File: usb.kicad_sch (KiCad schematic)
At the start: 29 parts, among them J3 USB-C_USB4105-GF-A, U11 TPD4E05U06QDQARQ1, U5 FT230X_QFN, U8 NCP730BMT330_WSON

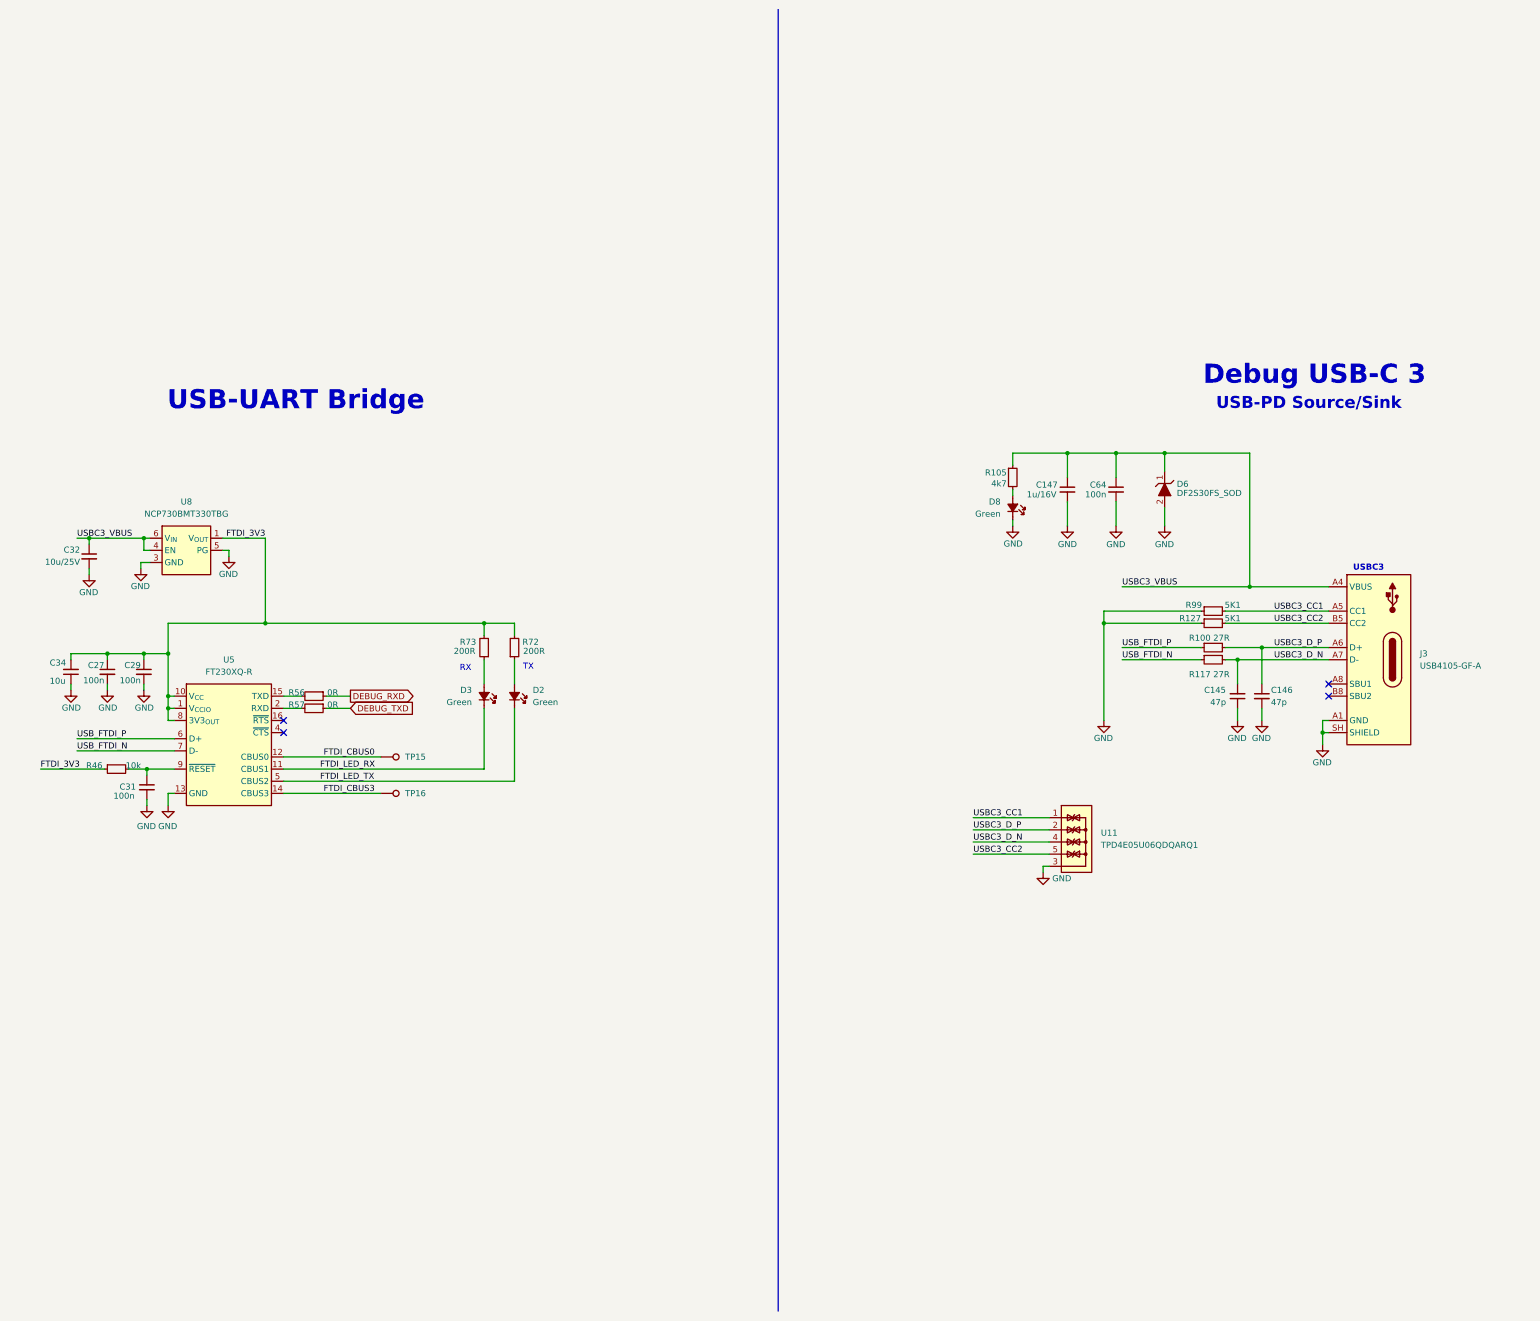
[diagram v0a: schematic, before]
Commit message: Schematic Cleanup, Complete routing
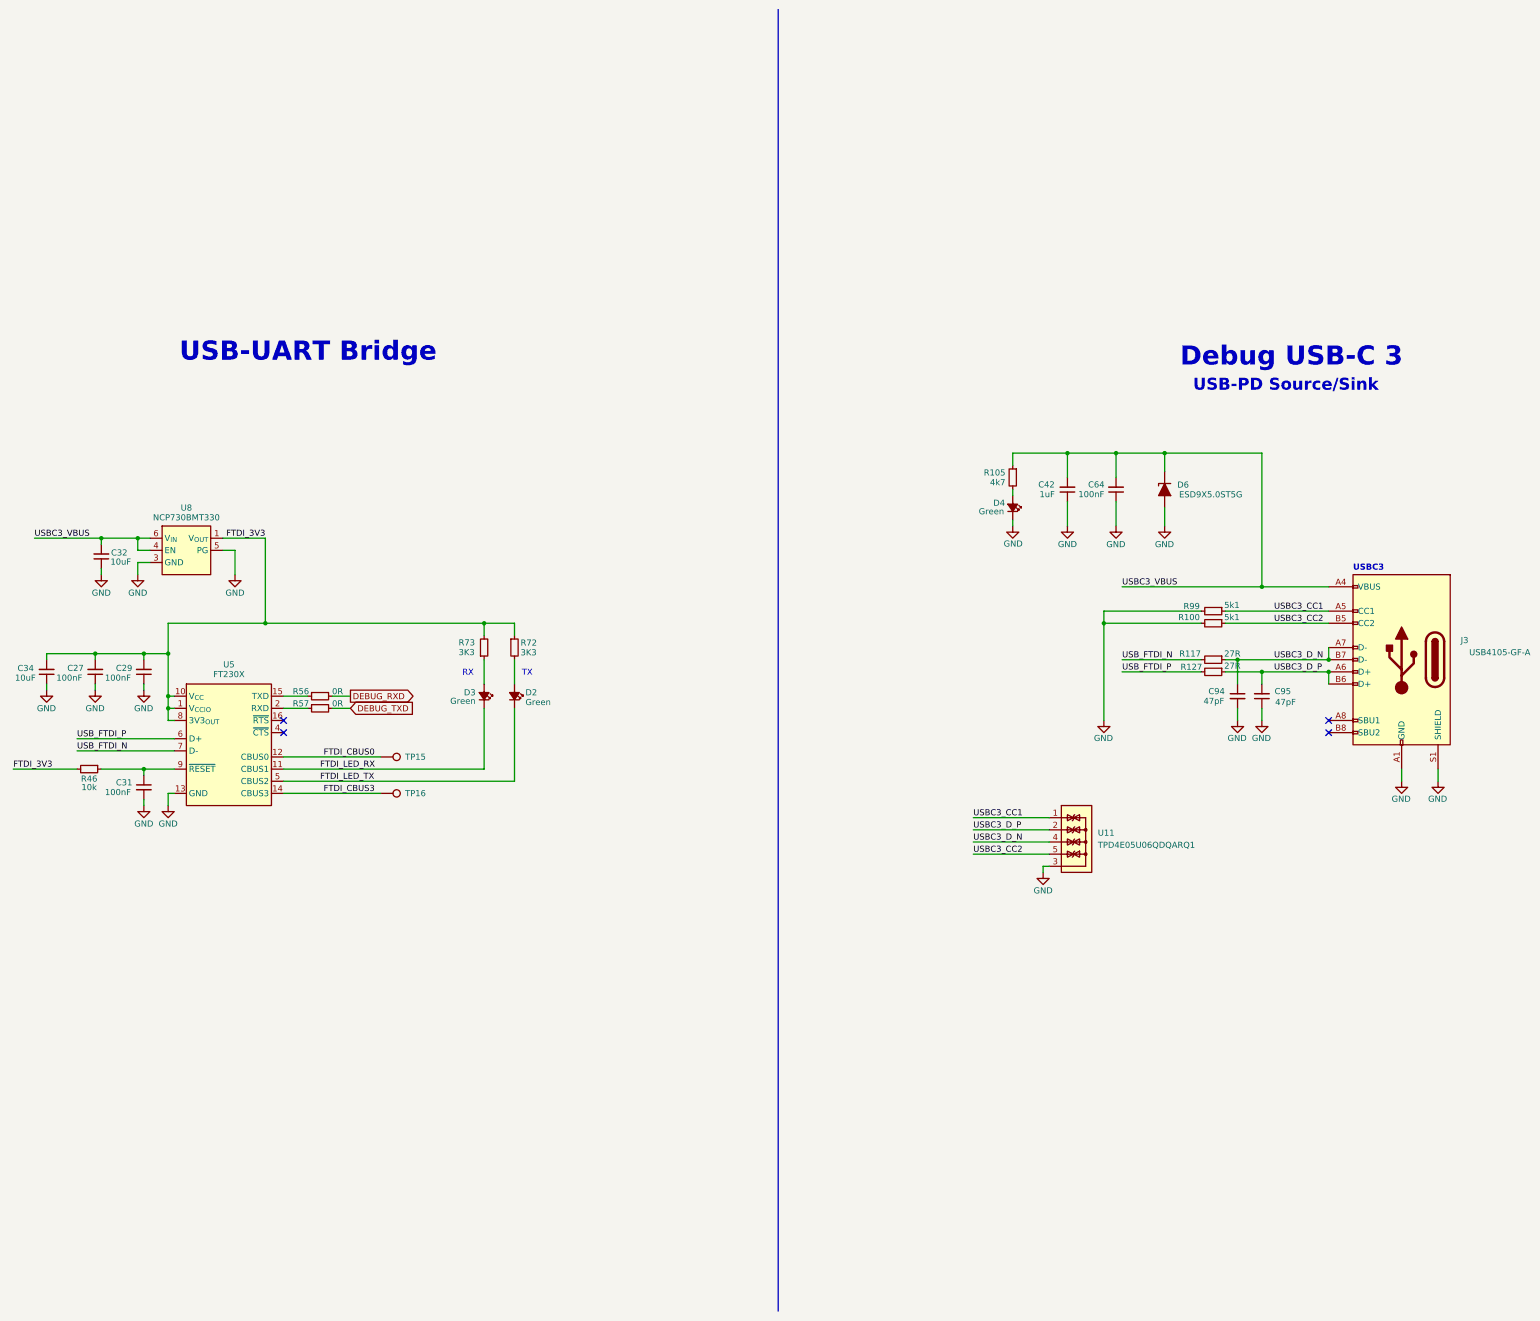
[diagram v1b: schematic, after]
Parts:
- C27, C29, C31, C64: value C_100n_0603 -> 100nF; symbol antmicroCapacitors0402:C_100n_0402 -> Device:C_Small
- C32: value C_10u_25V_0603 -> 10uF; symbol antmicroCapacitors0603:C_10u_25V_0603 -> Device:C_Small
- C34: value C_10u_0603 -> 10uF; symbol antmicroCapacitors0402:C_10u_0402 -> Device:C_Small
- C42: renamed from C147; value C_1u_16V_0603 -> 1uF; symbol antmicroCapacitors0402:C_1u_16V_0402 -> Device:C_Small
- C94: renamed from C145; value C_47p_0402 -> 47pF; symbol antmicroCapacitors0402:C_47p_0402 -> Device:C_Small
- C95: renamed from C146; value C_47p_0402 -> 47pF; symbol antmicroCapacitors0402:C_47p_0402 -> Device:C_Small
- D2, D3: symbol antmicroLEDIndicationDiscrete:LED_G_0603_LTST-C190GKT -> Device:LED_Small_Filled
- D4: renamed from D8; symbol antmicroLEDIndicationDiscrete:LED_G_0603_LTST-C190GKT -> Device:LED_Small_Filled
- D6: value DF2S30FS_SOD -> ESD9X5.0ST5G; symbol antmicroTVSDiodes:DF2S30FS_SOD -> Device:D_Zener_Filled
- J3: value USB-C_USB4105-GF-A -> USB4105-GF-A; symbol antmicroUSBConnectors:USB-C_GCT_USB4105-GF-A -> Connector:USB_C_Receptacle_USB2.0_16P
- R100: value R_5K1_0402 -> 5k1; symbol antmicroResistors0402:R_27R_0402 -> Device:R_Small; MPN CR0402-FX-27R0GLF -> (none); Manufacturer Bourns -> (none); Val 27R -> (none)
- R105: value R_4k7_0603 -> 4k7; symbol antmicroResistors0402:R_4k7_0402 -> Device:R_Small
- R117: value R_27R_0603 -> 27R; symbol antmicroResistors0402:R_27R_0402 -> Device:R_Small
- R127: value R_27R_0603 -> 27R; symbol antmicroResistors0402:R_27R_0402 -> Device:R_Small; Val 5K1 -> (none)
- R46: value R_10k_0603 -> 10k; symbol antmicroResistors0402:R_10k_0402 -> Device:R_Small
- R56, R57: value R_0R_0402 -> 0R; symbol antmicroResistors0402:R_0R_0402 -> Device:R_Small
- R72, R73: value R_200R_0603 -> 3K3; symbol antmicroResistors0402:R_200R_0402 -> Device:R_Small; MPN CR0402-FX-2000GLF -> (none); Manufacturer Bourns -> (none); Val 200R -> 3K3
- R99: value R_5K1_0603 -> 5k1; symbol antmicroResistors0402:R_27R_0402 -> Device:R_Small; MPN CR0402-FX-27R0GLF -> (none); Val 5K1 -> (none)
- TP15, TP16: symbol antmicroTestPoints:TP_0.75mm_SMD -> Connector:TestPoint
- U11: symbol antmicroTVSDiodes:TPD4E05U06QDQARQ1 -> JetsonCarrier:TPD4E05U06QDQARQ1
- U5: value FT230X_QFN -> FT230X; symbol antmicroInterfaceControllers:FT230X_QFN -> JetsonCarrier:FT230XQ
- U8: value NCP730BMT330_WSON -> NCP730BMT330; symbol antmicroPMICVoltageRegulatorsLinear:NCP730BMT330_WSON -> JetsonCarrier:NCP730BMT330
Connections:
- net DEBUG_RXD: now also R56.2; no longer R56.1
- net DEBUG_TXD: now also R57.2; no longer R57.1
- net FTDI_3V3: now also C27.2, C29.2, R46.2, R72.1; no longer C27.1, C29.1, R46.1, R72.2
- net GND: now also C27.1, C29.1, C32.1, C42.1, C64.1, C94.2, C95.1, J3.S1 (SHIELD), R100.2, R99.2; no longer C27.2, C29.2, C32.2, C42.2, C64.2, C94.1, C95.2, J3.SH (SHIELD), R100.1, R99.1
- net USBC3_CC1: now also R99.1; no longer R99.2
- net USBC3_CC2: now also R100.1; no longer R100.2
- net USBC3_D_N: now also C94.1, R117.1; no longer C94.2, R117.2
- net USBC3_D_P: now also C95.2, R127.1; no longer C95.1, R127.2
- net USBC3_VBUS: now also C32.2, C42.2, C64.2; no longer C32.1, C42.1, C64.1
- net USB_FTDI_N: now also R117.2; no longer R117.1
- net USB_FTDI_P: now also R127.2; no longer R127.1
- net at U5.15 (TXD): now also R56.1; no longer R56.2
- net at D2.2 (A): now also R72.2; no longer R72.1
- net at C31.1, U5.9 (~{RESET}): now also R46.1; no longer R46.2
- net at U5.2 (RXD): now also R57.1; no longer R57.2
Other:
- moved on the sheet: C27, C29, C31, C32, C34, C42, C64, C94, C95, R100, R105, R117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

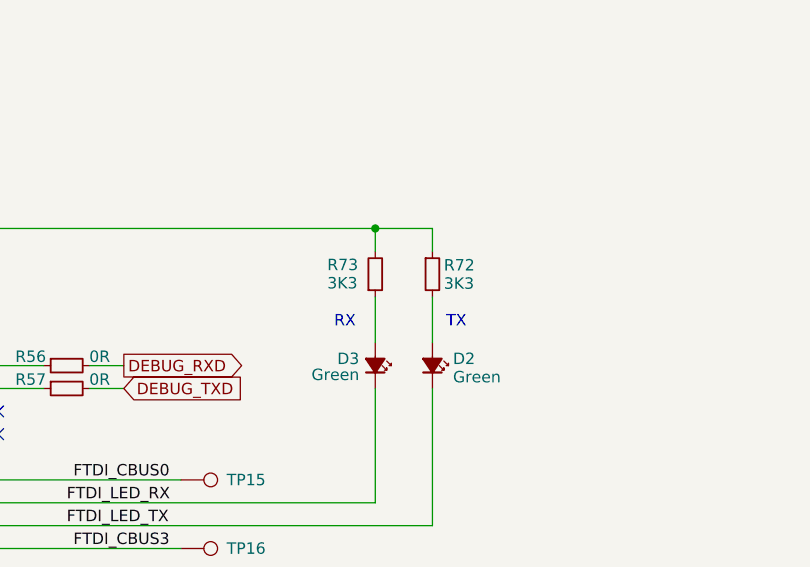
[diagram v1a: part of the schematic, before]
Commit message: Complete Silkscreen
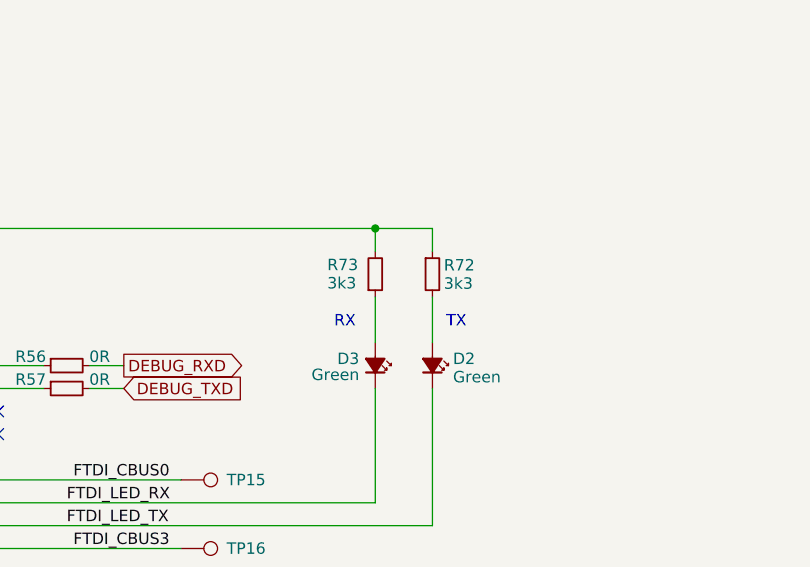
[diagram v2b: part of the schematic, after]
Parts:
- R72, R73: value 3K3 -> 3k3
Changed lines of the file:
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@@
 			)
 		)
-		(property "Value" "3K3"
+		(property "Value" "3k3"
 			(at 156.21 147.828 0)
 			(effects
@@
 			)
 		)
-		(property "Value" "3K3"
+		(property "Value" "3k3"
 			(at 143.256 146.304 0)
 			(effects
